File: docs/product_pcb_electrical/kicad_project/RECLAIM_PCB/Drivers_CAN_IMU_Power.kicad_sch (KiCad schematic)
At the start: 36 parts, among them U10 INA226AIDGST, U5L DRV8243SQDGQRQ1, U5R DRV8243SQDGQRQ1, U6A SN65HVD230DR, U6S SN65HVD230DR, U7 ICM-42688-P, U8 INA226AIDGST, U9 INA226AIDGST

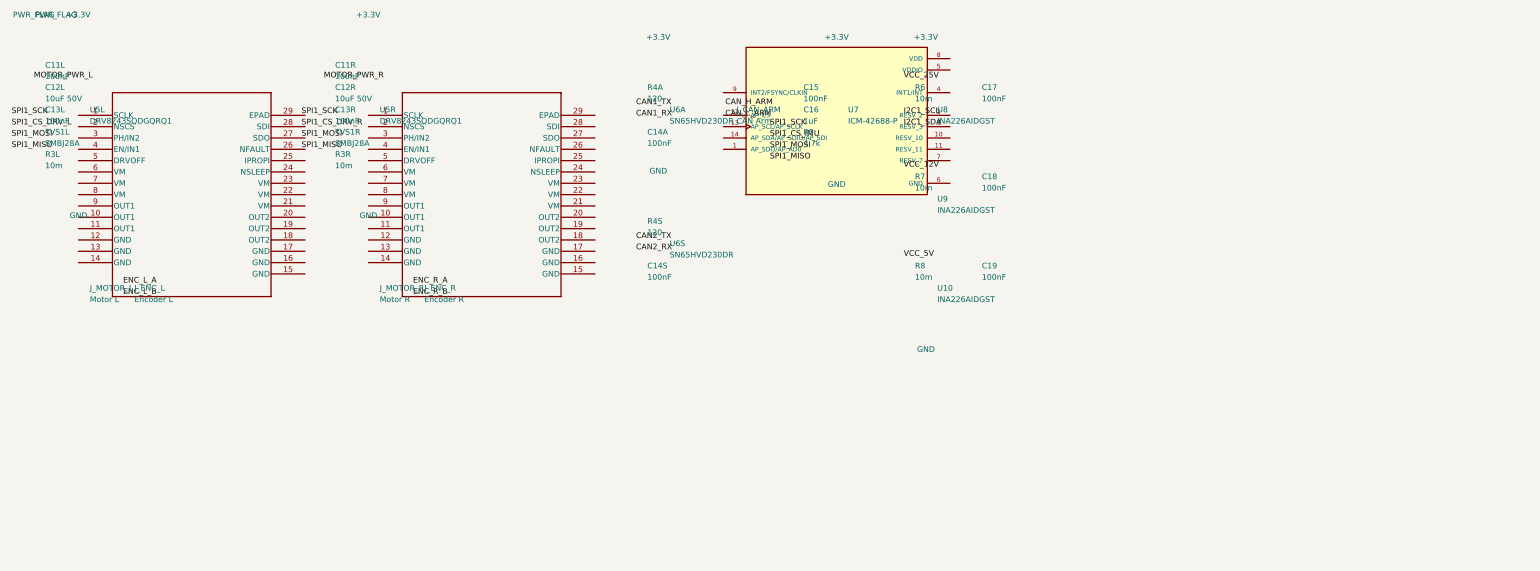
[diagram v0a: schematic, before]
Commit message: Add prototype schematic + tighten product layout to A3
Product: All 4 sub-sheets resized A2/A1→A3, components repositioned
into tight logical groups, duplicate K1/Q1 removed.

Prototype: New KiCad project with 3 hierarchical sheets
(Power, Teensy/Motor Control, Peripherals/Sensors), BOM, and
netlist reflecting as-built wiring: MD13C R3 + BTS7960 asymmetric
drivers, DC disconnect, 6-way fuse block, XINGYHENG servo buck.

Co-Authored-By: Claude Opus 4.6 <noreply@anthropic.com>
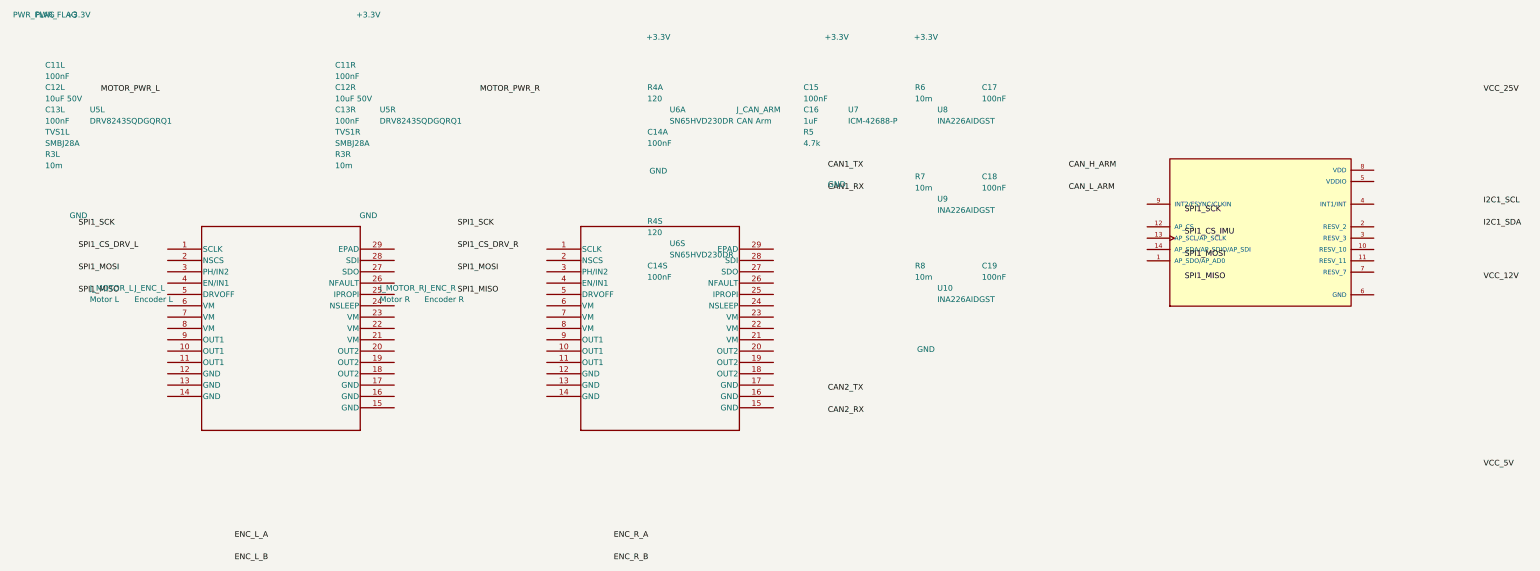
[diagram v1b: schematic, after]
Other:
- moved on the sheet: U5L, U5R, U7
